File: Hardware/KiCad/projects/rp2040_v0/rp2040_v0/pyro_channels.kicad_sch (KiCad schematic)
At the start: 26 parts, among them J15 Conn_01x02, J25 Screw_Terminal_01x02, J27 Screw_Terminal_01x02, J28 Screw_Terminal_01x02, Q2 AO3400A, Q4 AO3400A, Q5 AO3400A

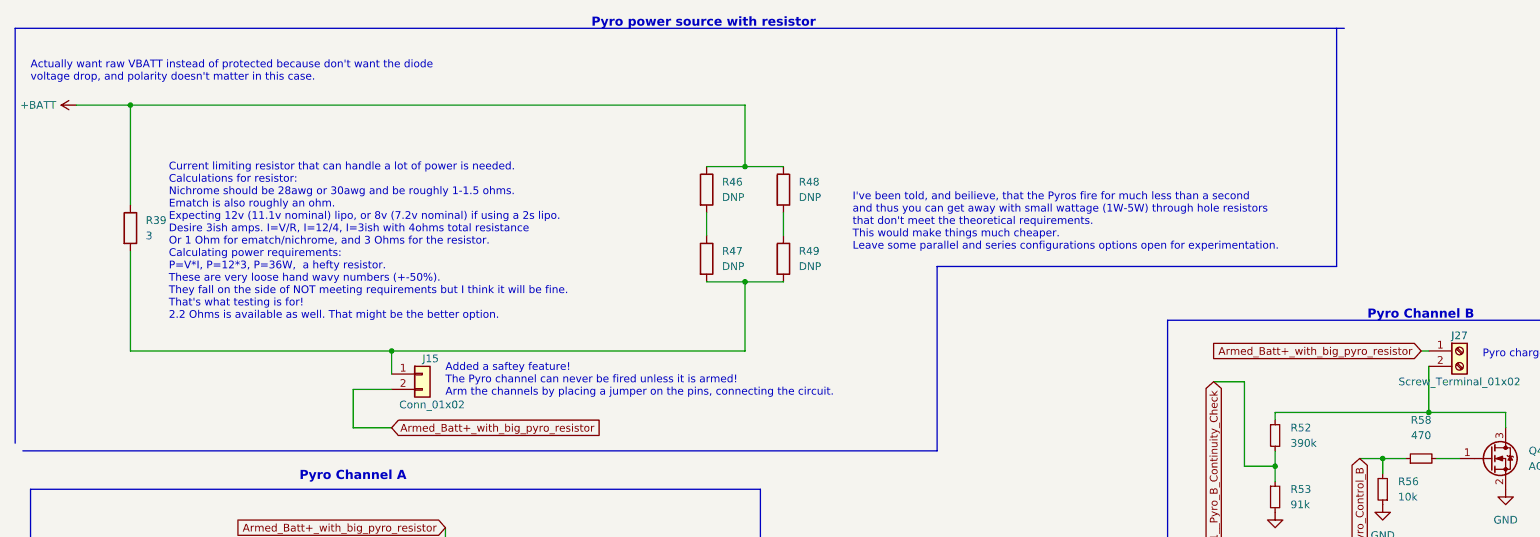
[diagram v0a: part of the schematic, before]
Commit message: MAKE SURE SAFTEY ARMING JUMPER IS BEFORE THE RESISTORS. Don't leave any hot wires exposed.
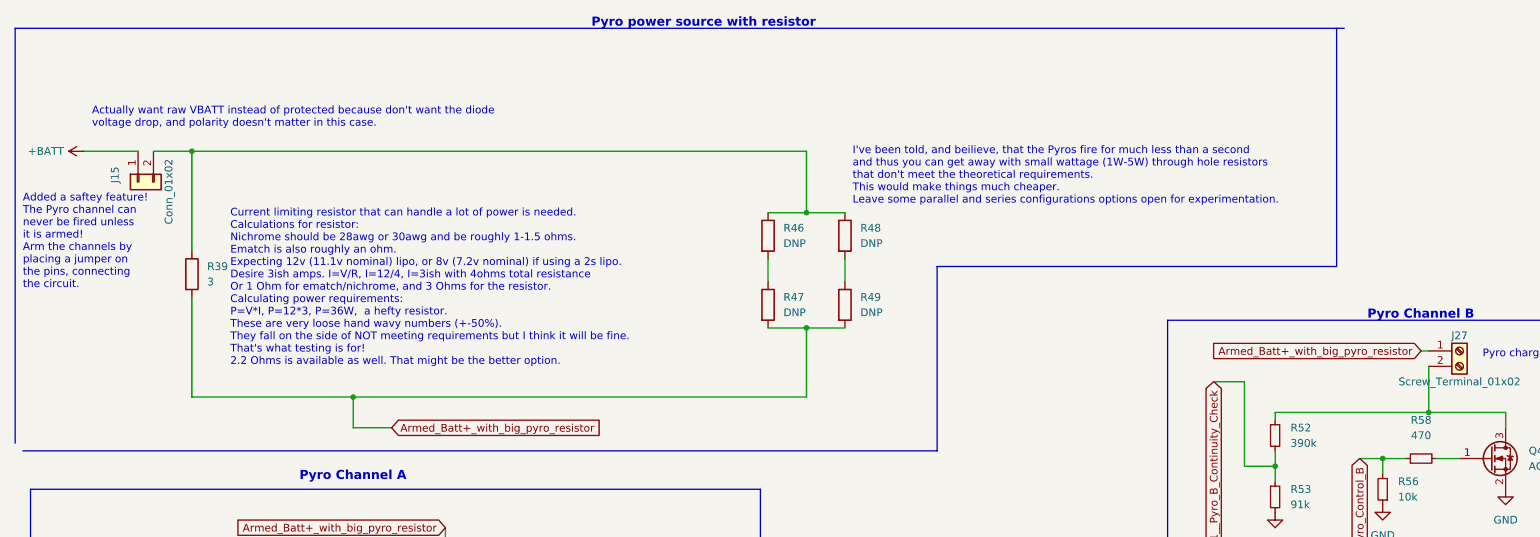
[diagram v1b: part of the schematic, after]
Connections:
- net +BATT: now also J15.1 (Pin_1); no longer R39.1, R46.1, R48.1
- net Armed_Batt+_with_big_pyro_resistor: now also R39.2, R47.2, R49.2; no longer J15.2 (Pin_2)
- new net: J15.2 (Pin_2), R39.1, R46.1, R48.1
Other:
- moved on the sheet: J15, R39, R46, R47, R48, R49
